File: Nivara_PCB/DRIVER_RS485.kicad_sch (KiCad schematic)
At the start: 7 parts, among them U6 RSM3485ECHT_C2992406

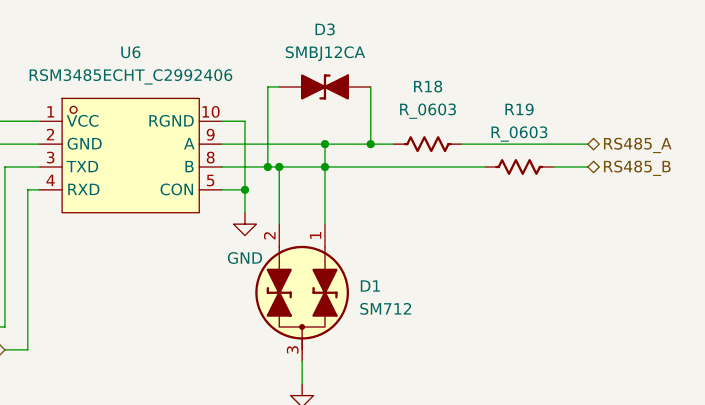
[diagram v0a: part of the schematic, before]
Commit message: Cambio de IntelliFet, porque los que tenían no estaban disponibles.
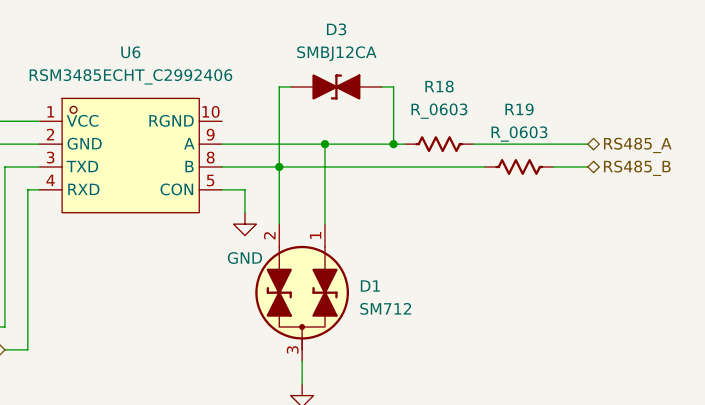
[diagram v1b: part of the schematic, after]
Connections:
- net GND: no longer U6.10 (RGND)
- net at D1.2 (A2), D3.1 (K), R19.1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: no longer D1.1 (A1), D3.2 (A), R18.1, U6.9 (A)
- new net: D1.1 (A1), D3.2 (A), R18.1, U6.9 (A)
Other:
- moved on the sheet: D3, R18
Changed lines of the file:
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@@
 	)
 	(junction
-		(at 74.93 67.31)
+		(at 39.37 72.39)
 		(diameter 0)
 		(color 0 0 0 0)
 	)
 	(junction
-		(at 88.9 62.23)
+		(at 91.44 62.23)
+		(diameter 0)
+		(color 0 0 0 0)
+	)
+	(junction
+		(at 39.37 59.69)
 		(diameter 0)
 		(color 0 0 0 0)
@@
 		(color 0 0 0 0)
 	)
-	(junction
-		(at 39.37 72.39)
-		(diameter 0)
-		(color 0 0 0 0)
-	)
-	(junction
-		(at 83.82 64.77)
-		(diameter 0)
-		(color 0 0 0 0)
-	)
-	(junction
-		(at 77.47 64.77)
-		(diameter 0)
-		(color 0 0 0 0)
-	)
-	(junction
-		(at 39.37 59.69)
-		(diameter 0)
-		(color 0 0 0 0)
-	)
 	(wire
 		(pts
@@
 	(wire
 		(pts
-			(xy 83.82 62.23) (xy 83.82 64.77)
-		)
-		(stroke
-			(width 0)
-			(type default)
-		)
-	)
-	(wire
-		(pts
-			(xy 74.93 59.69) (xy 74.93 67.31)
-		)
-		(stroke
-			(width 0)
-			(type default)
-		)
-	)
-	(wire
-		(pts
-			(xy 72.39 59.69) (xy 74.93 59.69)
+			(xy 91.44 62.23) (xy 92.71 62.23)
 		)
 		(stroke
@@
 	(wire
 		(pts
-			(xy 83.82 64.77) (xy 83.82 71.12)
-		)
-		(stroke
-			(width 0)
-			(type default)
-		)
-	)
-	(wire
-		(pts
-			(xy 83.82 64.77) (xy 78.74 64.77)
+			(xy 78.74 64.77) (xy 101.6 64.77)
 		)
 		(stroke
@@
 	(wire
 		(pts
-			(xy 72.39 64.77) (xy 77.47 64.77)
+			(xy 72.39 64.77) (xy 78.74 64.77)
 		)
 		(stroke
@@
 	(wire
 		(pts
-			(xy 78.74 55.88) (xy 77.47 55.88)
-		)
-		(stroke
-			(width 0)
-			(type default)
-		)
-	)
-	(wire
-		(pts
-			(xy 77.47 55.88) (xy 77.47 64.77)
+			(xy 80.01 55.88) (xy 78.74 55.88)
+		)
+		(stroke
+			(width 0)
+			(type default)
+		)
+	)
+	(wire
+		(pts
+			(xy 78.74 55.88) (xy 78.74 64.77)
 		)
 		(stroke
@@
 	(wire
 		(pts
-			(xy 77.47 64.77) (xy 78.74 64.77)
-		)
-		(stroke
-			(width 0)
-			(type default)
-		)
-	)
-	(wire
-		(pts
 			(xy 50.8 85.09) (xy 50.8 67.31)
 		)
@@
 	(wire
 		(pts
-			(xy 99.06 62.23) (xy 113.03 62.23)
+			(xy 100.33 62.23) (xy 113.03 62.23)
 		)
 		(stroke
@@
 	(wire
 		(pts
+			(xy 83.82 62.23) (xy 91.44 62.23)
+		)
+		(stroke
+			(width 0)
+			(type default)
+		)
+	)
+	(wire
+		(pts
 			(xy 39.37 59.69) (xy 39.37 62.23)
 		)
@@
 	(wire
 		(pts
-			(xy 88.9 55.88) (xy 88.9 62.23)
+			(xy 83.82 62.23) (xy 83.82 71.12)
+		)
+		(stroke
+			(width 0)
+			(type default)
+		)
+	)
+	(wire
+		(pts
+			(xy 91.44 55.88) (xy 91.44 62.23)
 		)
 		(stroke
@@
 	(wire
 		(pts
+			(xy 90.17 55.88) (xy 91.44 55.88)
+		)
+		(stroke
+			(width 0)
+			(type default)
+		)
+	)
+	(wire
+		(pts
 			(xy 45.72 72.39) (xy 45.72 62.23)
 		)
@@
 	(wire
 		(pts
-			(xy 83.82 64.77) (xy 101.6 64.77)
-		)
-		(stroke
-			(width 0)
-			(type default)
-		)
-	)
-	(wire
-		(pts
-			(xy 88.9 62.23) (xy 91.44 62.23)
-		)
-		(stroke
-			(width 0)
-			(type default)
-		)
-	)
-	(wire
-		(pts
 			(xy 48.26 64.77) (xy 48.26 82.55)
-		)
-		(stroke
-			(width 0)
-			(type default)
-		)
-	)
-	(wire
-		(pts
-			(xy 83.82 62.23) (xy 88.9 62.23)
 		)
 		(stroke
@@
 	(symbol
 		(lib_id "PCM_Resistor_US_AKL:R_0603")
-		(at 95.25 62.23 90)
+		(at 96.52 62.23 90)
 		(unit 1)
 		(exclude_from_sim no)
@@
 		(fields_autoplaced yes)
 		(property "Reference" "R18"
-			(at 95.25 55.88 90)
+			(at 96.52 55.88 90)
 			(effects
 				(font
@@
 		)
 		(property "Value" "R_0603"
-			(at 95.25 58.42 90)
+			(at 96.52 58.42 90)
 			(effects
 				(font
@@
 		)
 		(property "Footprint" "PCM_Resistor_SMD_AKL:R_0603_1608Metric"
-			(at 106.68 62.23 0)
+			(at 107.95 62.23 0)
 			(effects
 				(font
@@
 		)
 		(property "Datasheet" "~"
-			(at 95.25 62.23 0)
+			(at 96.52 62.23 0)
 			(effects
 				(font
@@
 		)
 		(property "Description" "SMD 0603 Chip Resistor, US Symbol, Alternate KiCad Library"
-			(at 95.25 62.23 0)
+			(at 96.52 62.23 0)
 			(effects
 				(font
@@
 	(symbol
 		(lib_id "PCM_Diode_TVS_AKL:SMBJ12CA")
-		(at 83.82 55.88 0)
+		(at 85.09 55.88 0)
 		(unit 1)
 		(exclude_from_sim no)
@@
 		(fields_autoplaced yes)
 		(property "Reference" "D3"
-			(at 83.82 49.53 0)
+			(at 85.09 49.53 0)
 			(effects
 				(font
@@
 		)
 		(property "Value" "SMBJ12CA"
-			(at 83.82 52.07 0)
+			(at 85.09 52.07 0)
 			(effects
 				(font
@@
 		)
 		(property "Footprint" "PCM_Diode_SMD_AKL:D_SMB_TVS"
-			(at 83.82 55.88 0)
+			(at 85.09 55.88 0)
 			(effects
 				(font
@@
 		)
 		(property "Datasheet" "https://www.tme.eu/Document/0b6222bec7e12d83185b51d73cb6a54d/SMBJ_ser.pdf"
-			(at 83.82 55.88 0)
+			(at 85.09 55.88 0)
 			(effects
 				(font
@@
 		)
 		(property "Description" "SMB Bidirectional TVS Diode, 12V, 600W, Alternate KiCAD Library"
-			(at 83.82 55.88 0)
-			(effects
-				(font
+			(at 85.09 55.88 0)
+			(effects
+				(font

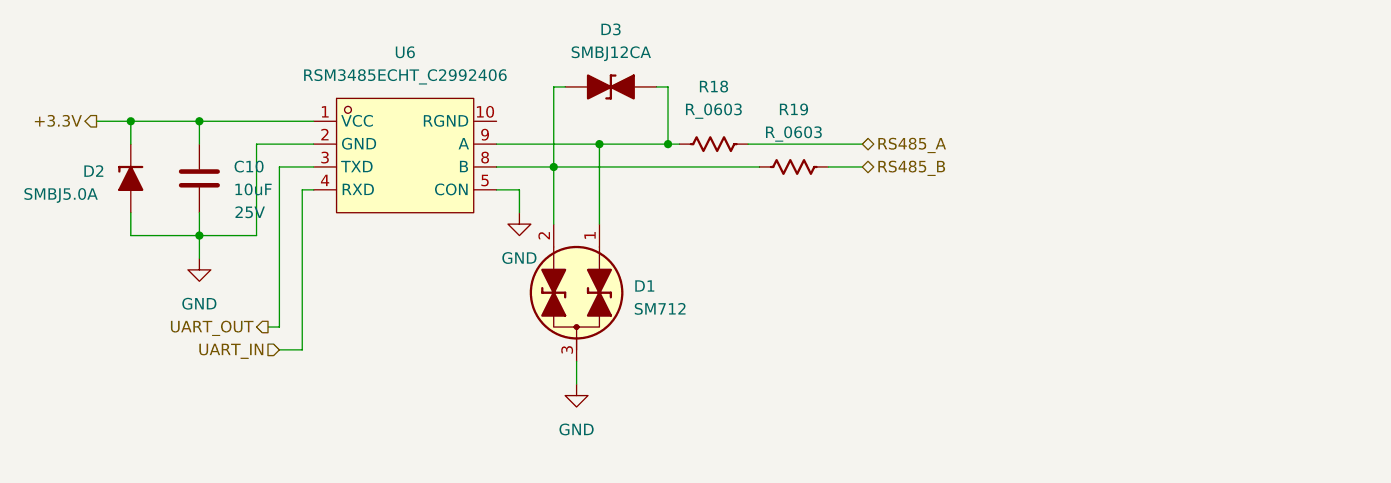
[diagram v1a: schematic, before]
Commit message: Cambios en las salidas analogicas, ya que el ESP32 S3 no tiene DAC
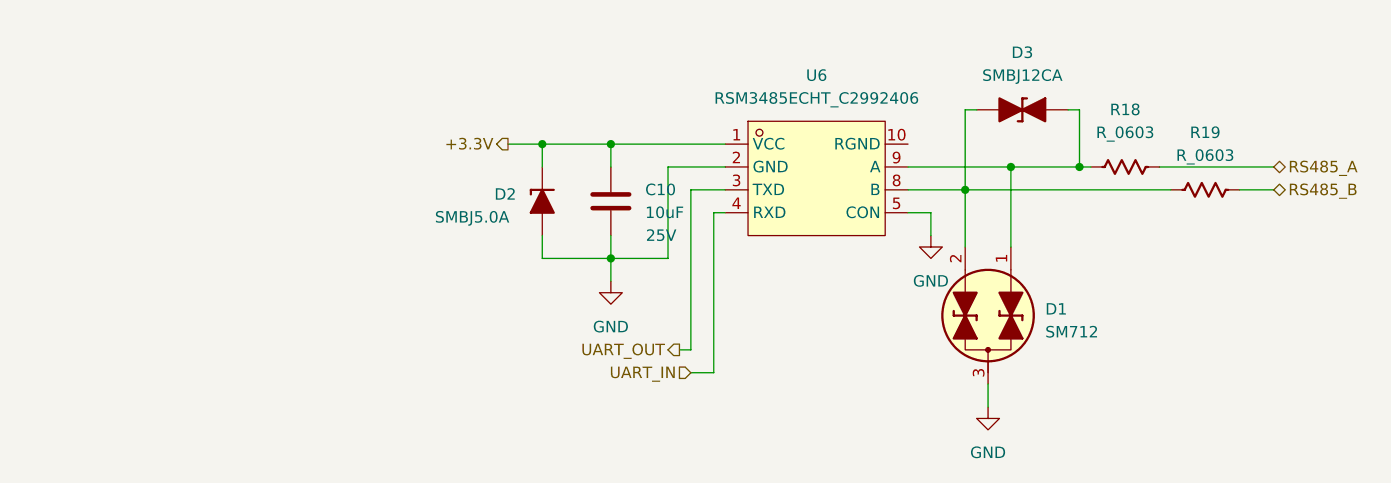
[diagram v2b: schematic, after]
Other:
- moved on the sheet: C10, D1, D2, D3, R18, R19, U6

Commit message: Cambios en la medición de voltaje y corriente de la PCB Nivara.
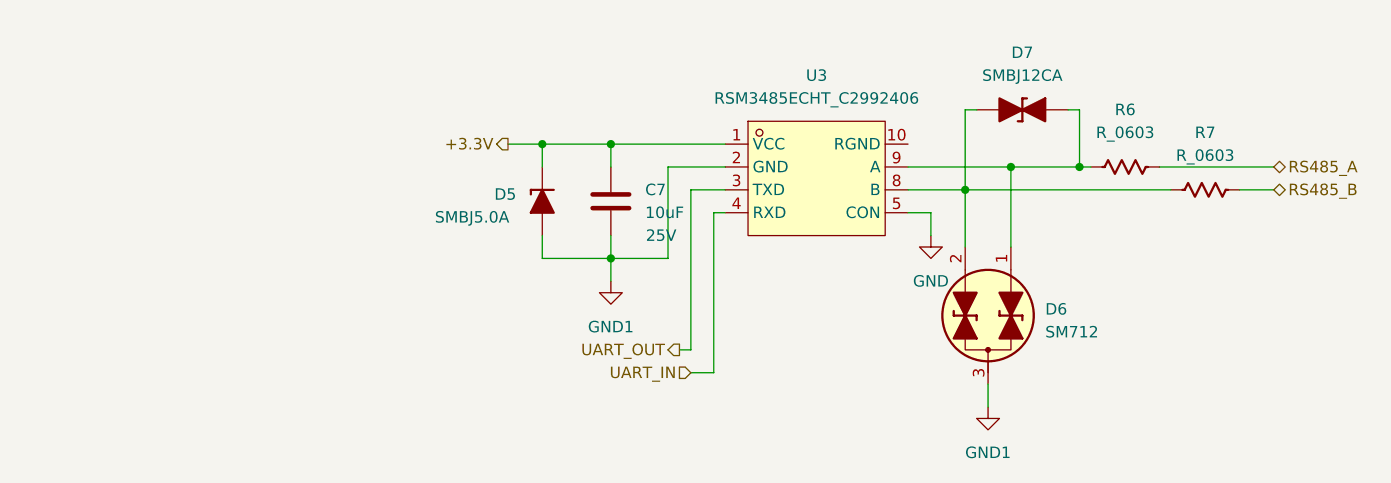
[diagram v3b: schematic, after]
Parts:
- removed U6: RSM3485ECHT_C2992406, Fuse_Holder:COMM-TH_8P-L19.5-W16.5-P2.54-BL, symbol Fuse_Holder:RSM3485ECHT_C2992406
- added U3: RSM3485ECHT_C2992406, EasyEDA:COMM-TH_8P-L19.5-W16.5-P2.54-BL, symbol EasyEDA:RSM3485ECHT_C2992406
- renumbered C10 to C7, D2 to D5, D1 to D6, D3 to D7, R18 to R6, R19 to R7
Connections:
- net +3.3V: now also U3.1 (VCC)
- net GND: now also U3.5 (CON); no longer C7.2, D5.2 (A), D6.3 (Com)
- net UART_IN: now also U3.4 (RXD)
- net UART_OUT: now also U3.3 (TXD)
- net at D6.2 (A2), D7.1 (K), R7.1: now also U3.8 (B)
- net at D6.1 (A1), D7.2 (A), R6.1: now also U3.9 (A)
- new net GND1: C7.2, D5.2 (A), D6.3 (Com), U3.2 (GND)

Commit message: Cambios en el PCB de Nivara. Ruteo de emtradas y salidas NPN y PNP.
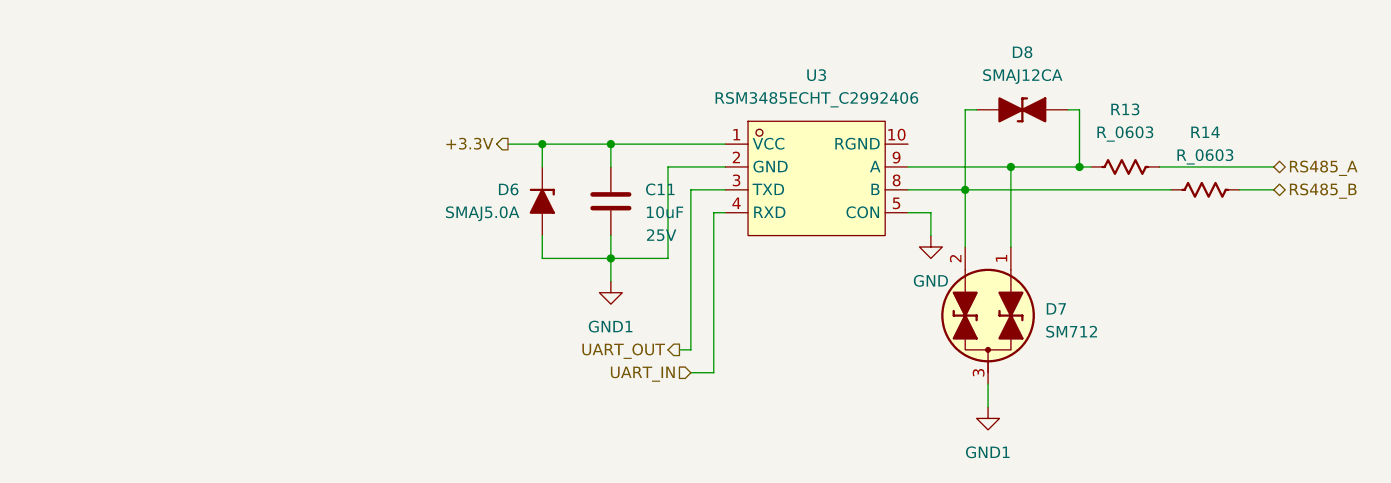
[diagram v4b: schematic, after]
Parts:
- removed D5: SMBJ5.0A, PCM_Diode_SMD_AKL:D_SMB, symbol PCM_Diode_TVS_AKL:SMBJ5.0A
- removed D7: SMBJ12CA, PCM_Diode_SMD_AKL:D_SMB_TVS, symbol PCM_Diode_TVS_AKL:SMBJ12CA
- added D6: SMAJ5.0A, PCM_Diode_SMD_AKL:D_SMA, symbol PCM_Diode_TVS_AKL:SMAJ5.0A
- added D8: SMAJ12CA, PCM_Diode_SMD_AKL:D_SMA_TVS, symbol PCM_Diode_TVS_AKL:SMAJ12CA
- renumbered C7 to C11, D6 to D7, R6 to R13, R7 to R14
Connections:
- net +3.3V: now also D6.1 (K)
- net GND1: now also D6.2 (A)
- net at D7.1 (A1), R13.1, U3.9 (A): now also D8.2 (A)
- net at D7.2 (A2), R14.1, U3.8 (B): now also D8.1 (K)
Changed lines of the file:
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@@
 		(on_board yes)
 		(dnp no)
-		(property "Reference" "C7"
+		(property "Reference" "C11"
 			(at 88.9 67.3099 0)
 			(effects
@@
 			(project "Nivara_PCB"
 				(path "/13184db0-a71d-4054-b13a-bbf46d2b100d/4e7fa7f2-8bf5-4f9c-874d-fa1b4fd76f92/3eeaffcc-9bb5-4f36-a3b6-9bf8c04eaeb0"
-					(reference "C7")
-					(unit 1)
-				)
-			)
-		)
-	)
-	(symbol
-		(lib_id "PCM_Diode_TVS_AKL:SMBJ5.0A")
-		(at 77.47 68.58 90)
-		(unit 1)
-		(exclude_from_sim no)
-		(in_bom yes)
-		(on_board yes)
-		(dnp no)
-		(property "Reference" "D5"
-			(at 72.136 67.818 90)
+					(reference "C11")
+					(unit 1)
+				)
+			)
+		)
+	)
+	(symbol
+		(lib_id "PCM_Diode_TVS_AKL:SMAJ5.0A")
+		(at 77.47 68.58 270)
+		(mirror x)
+		(unit 1)
+		(exclude_from_sim no)
+		(in_bom yes)
+		(on_board yes)
+		(dnp no)
+		(property "Reference" "D6"
+			(at 74.93 67.3099 90)
 			(effects
 				(font
@@
 			)
 		)
-		(property "Value" "SMBJ5.0A"
-			(at 65.532 70.358 90)
+		(property "Value" "SMAJ5.0A"
+			(at 74.93 69.8499 90)
 			(effects
 				(font
@@
 			)
 		)
-		(property "Footprint" "PCM_Diode_SMD_AKL:D_SMB"
+		(property "Footprint" "PCM_Diode_SMD_AKL:D_SMA"
 			(at 77.47 68.58 0)
 			(effects
@@
 			)
 		)
-		(property "Datasheet" "https://www.tme.eu/Document/0b6222bec7e12d83185b51d73cb6a54d/SMBJ_ser.pdf"
+		(property "Datasheet" "https://www.tme.eu/Document/dbc72d81c249fe51b6ab42300e8e06d0/SMAJ_ser.pdf"
 			(at 77.47 68.58 0)
 			(effects
@@
 			)
 		)
-		(property "Description" "SMB Unidirectional TVS diode, 5V, 600W, Alternate KiCAD Library"
+		(property "Description" "SMA Unidirectional TVS diode, 5V, 400W, Alternate KiCAD Library"
 			(at 77.47 68.58 0)
 			(effects
@@
 			(project ""
 				(path "/13184db0-a71d-4054-b13a-bbf46d2b100d/4e7fa7f2-8bf5-4f9c-874d-fa1b4fd76f92/3eeaffcc-9bb5-4f36-a3b6-9bf8c04eaeb0"
-					(reference "D5")
+					(reference "D6")
 					(unit 1)
 				)
@@
 		(dnp no)
 		(fields_autoplaced yes)
-		(property "Reference" "D6"
+		(property "Reference" "D7"
 			(at 133.35 80.5814 90)
 			(effects
@@
 			(project ""
 				(path "/13184db0-a71d-4054-b13a-bbf46d2b100d/4e7fa7f2-8bf5-4f9c-874d-fa1b4fd76f92/3eeaffcc-9bb5-4f36-a3b6-9bf8c04eaeb0"
-					(reference "D6")
+					(reference "D7")
 					(unit 1)
 				)
@@
 		(dnp no)
 		(fields_autoplaced yes)
-		(property "Reference" "R6"
+		(property "Reference" "R13"
 			(at 142.24 58.42 90)
 			(effects
@@
 			(project ""
 				(path "/13184db0-a71d-4054-b13a-bbf46d2b100d/4e7fa7f2-8bf5-4f9c-874d-fa1b4fd76f92/3eeaffcc-9bb5-4f36-a3b6-9bf8c04eaeb0"
-					(reference "R6")
+					(reference "R13")
+					(unit 1)
+				)
+			)
+		)
+	)
+	(symbol
+		(lib_id "PCM_Diode_TVS_AKL:SMAJ12CA")
+		(at 130.81 58.42 0)
+		(unit 1)
+		(exclude_from_sim no)
+		(in_bom yes)
+		(on_board yes)
+		(dnp no)
+		(fields_autoplaced yes)
+		(property "Reference" "D8"
+			(at 130.81 52.07 0)
+			(effects
+				(font
+					(size 1.27 1.27)
+				)
+			)
+		)
+		(property "Value" "SMAJ12CA"
+			(at 130.81 54.61 0)
+			(effects
+				(font
+					(size 1.27 1.27)
+				)
+			)
+		)
+		(property "Footprint" "PCM_Diode_SMD_AKL:D_SMA_TVS"
+			(at 130.81 58.42 0)
+			(effects
+				(font
+					(size 1.27 1.27)
+				)
+				(hide yes)
+			)
+		)
+		(property "Datasheet" "https://www.tme.eu/Document/dbc72d81c249fe51b6ab42300e8e06d0/SMAJ_ser.pdf"
+			(at 130.81 58.42 0)
+			(effects
+				(font
+					(size 1.27 1.27)
+				)
+				(hide yes)
+			)
+		)
+		(property "Description" "SMA Bidirectional TVS Diode, 12V, 400W, Alternate KiCAD Library"
+			(at 130.81 58.42 0)
+			(effects
+				(font
+					(size 1.27 1.27)
+				)
+				(hide yes)
+			)
+		)
+		(pin "2"
+		)
+		(pin "1"
+		)
+		(instances
+			(project ""
+				(path "/13184db0-a71d-4054-b13a-bbf46d2b100d/4e7fa7f2-8bf5-4f9c-874d-fa1b4fd76f92/3eeaffcc-9bb5-4f36-a3b6-9bf8c04eaeb0"
+					(reference "D8")
 					(unit 1)
 				)
@@
 		(dnp no)
 		(fields_autoplaced yes)
-		(property "Reference" "#PWR024"
+		(property "Reference" "#PWR045"
 			(at 85.09 83.82 0)
 			(effects
@@
 			(project "Nivara_PCB"
 				(path "/13184db0-a71d-4054-b13a-bbf46d2b100d/4e7fa7f2-8bf5-4f9c-874d-fa1b4fd76f92/3eeaffcc-9bb5-4f36-a3b6-9bf8c04eaeb0"
-					(reference "#PWR024")
+					(reference "#PWR045")
 					(unit 1)
 				)
@@
 		(dnp no)
 		(fields_autoplaced yes)
-		(property "Reference" "R7"
+		(property "Reference" "R14"
 			(at 151.13 60.96 90)
 			(effects
@@
 			(project "Nivara_PCB"
 				(path "/13184db0-a71d-4054-b13a-bbf46d2b100d/4e7fa7f2-8bf5-4f9c-874d-fa1b4fd76f92/3eeaffcc-9bb5-4f36-a3b6-9bf8c04eaeb0"
-					(reference "R7")
+					(reference "R14")
 					(unit 1)
 				)
@@
 		(dnp no)
 		(fields_autoplaced yes)
-		(property "Reference" "#PWR026"
+		(property "Reference" "#PWR047"
 			(at 127 97.79 0)
 			(effects
@@
 			(project "Nivara_PCB"
 				(path "/13184db0-a71d-4054-b13a-bbf46d2b100d/4e7fa7f2-8bf5-4f9c-874d-fa1b4fd76f92/3eeaffcc-9bb5-4f36-a3b6-9bf8c04eaeb0"
-					(reference "#PWR026")
-					(unit 1)
-				)
-			)
-		)
-	)
-	(symbol
-		(lib_id "PCM_Diode_TVS_AKL:SMBJ12CA")
-		(at 130.81 58.42 0)
-		(unit 1)
-		(exclude_from_sim no)
-		(in_bom yes)
-		(on_board yes)
-		(dnp no)
-		(fields_autoplaced yes)
-		(property "Reference" "D7"
-			(at 130.81 52.07 0)
-			(effects
-				(font
-					(size 1.27 1.27)
-				)
-			)
-		)
-		(property "Value" "SMBJ12CA"
-			(at 130.81 54.61 0)
-			(effects
-				(font
-					(size 1.27 1.27)
-				)
-			)
-		)
-		(property "Footprint" "PCM_Diode_SMD_AKL:D_SMB_TVS"
-			(at 130.81 58.42 0)
-			(effects
-				(font
-					(size 1.27 1.27)
-				)
-				(hide yes)
-			)
-		)
-		(property "Datasheet" "https://www.tme.eu/Document/0b6222bec7e12d83185b51d73cb6a54d/SMBJ_ser.pdf"
-			(at 130.81 58.42 0)
-			(effects
-				(font
-					(size 1.27 1.27)
-				)
-				(hide yes)
-			)
-		)
-		(property "Description" "SMB Bidirectional TVS Diode, 12V, 600W, Alternate KiCAD Library"
-			(at 130.81 58.42 0)
-			(effects
-				(font
-					(size 1.27 1.27)
-				)
-				(hide yes)
-			)
-		)
-		(pin "2"
-		)
-		(pin "1"
-		)
-		(instances
-			(project ""
-				(path "/13184db0-a71d-4054-b13a-bbf46d2b100d/4e7fa7f2-8bf5-4f9c-874d-fa1b4fd76f92/3eeaffcc-9bb5-4f36-a3b6-9bf8c04eaeb0"
-					(reference "D7")
+					(reference "#PWR047")
 					(unit 1)
 				)
@@
 		(dnp no)
 		(fields_autoplaced yes)
-		(property "Reference" "#PWR025"
+		(property "Reference" "#PWR046"
 			(at 120.65 78.74 0)
 			(effects
@@
 			(project "Nivara_PCB"
 				(path "/13184db0-a71d-4054-b13a-bbf46d2b100d/4e7fa7f2-8bf5-4f9c-874d-fa1b4fd76f92/3eeaffcc-9bb5-4f36-a3b6-9bf8c04eaeb0"
-					(reference "#PWR025")
-					(unit 1)
-				)
+					(reference "#PWR046")
+					(unit 1)
+				)
